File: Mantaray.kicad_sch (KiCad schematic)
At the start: 0 parts

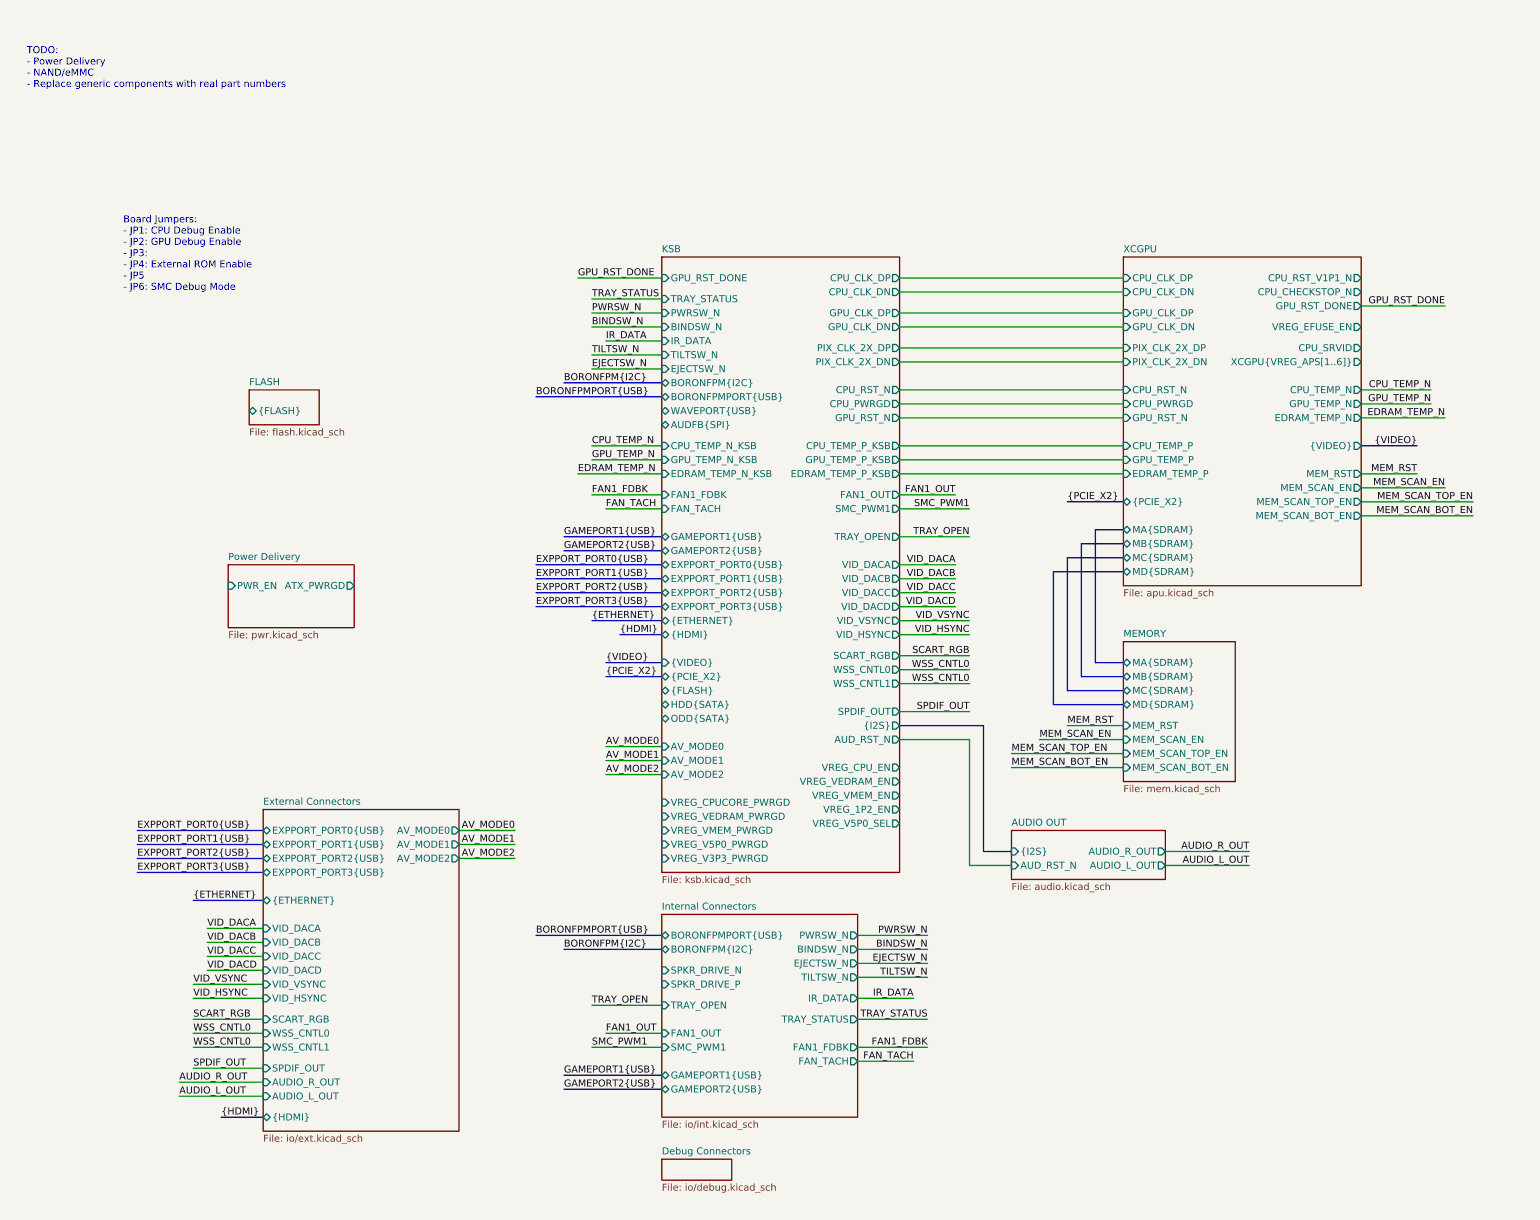
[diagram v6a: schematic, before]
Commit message: Nand Flash, Sata Connectors and removing (hopefully) unnecessary things
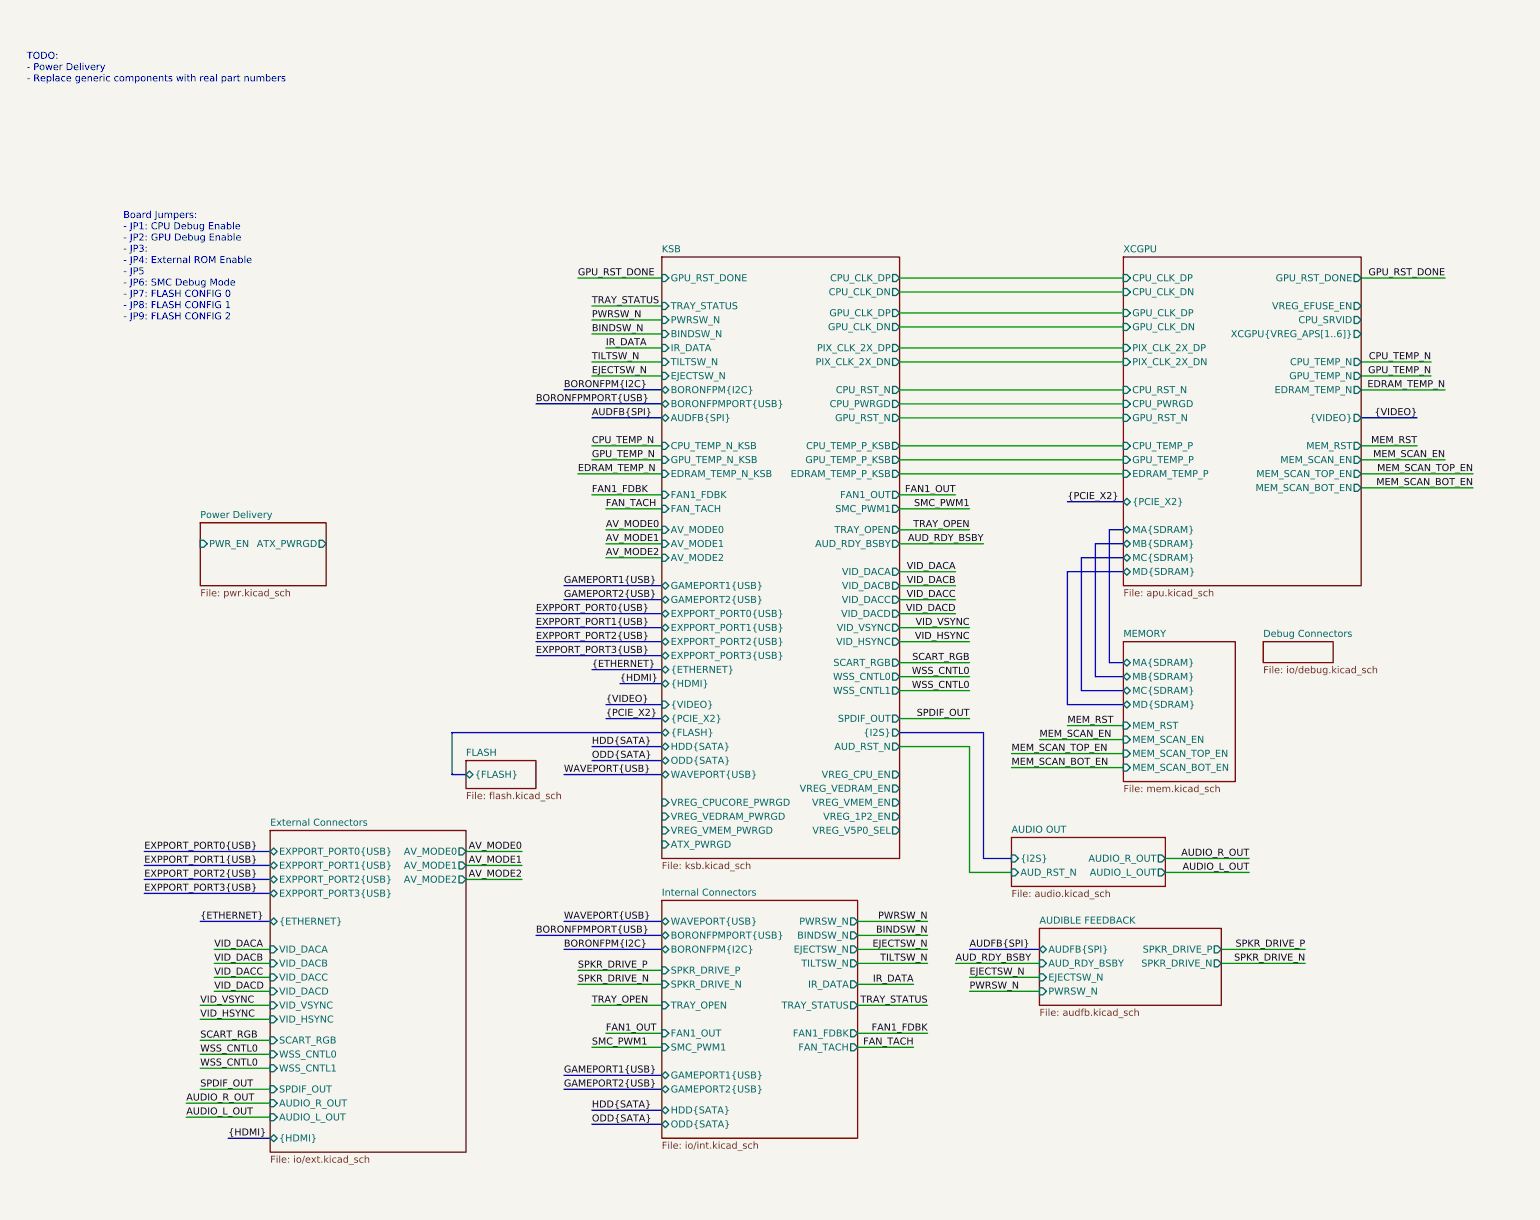
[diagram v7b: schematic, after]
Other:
- added sheet AUDIBLE FEEDBACK (audfb.kicad_sch)
- sheet Internal Connectors ports: added HDD{SATA}, ODD{SATA}, WAVEPORT{USB}; removed none
- sheet KSB ports: added ATX_PWRGD, AUD_RDY_BSBY; removed VREG_V3P3_PWRGD, VREG_V5P0_PWRGD
- sheet XCGPU ports: added none; removed CPU_CHECKSTOP_N, CPU_RST_V1P1_N
- note added: "Board Jumpers: - JP1: CPU Debug Enable - JP2: GPU Debug Enable - JP3: - JP4: External ROM Enable - JP5 - JP6: SMC Debug Mode - JP7: FLASH CONFIG 0 - JP8: FLASH CONFIG 1 - JP9: FLASH CONFIG 2"
- note added: "TODO: - Power Delivery - Replace generic components with real part numbers"
- note removed: "Board Jumpers: - JP1: CPU Debug Enable - JP2: GPU Debug Enable - JP3: - JP4: External ROM Enable - JP5 - JP6: SMC Debug Mode"
- note removed: "TODO: - Power Delivery - NAND/eMMC - Replace generic components with real part numbers"

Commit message: Multipurpose and standby power rails, Reannotated schematic
Added V_1P2, V_1P8, V_5P0DUAL, V_EFUSE, V_GPUPCIE, V_3P3STBY and V_1P2STBY
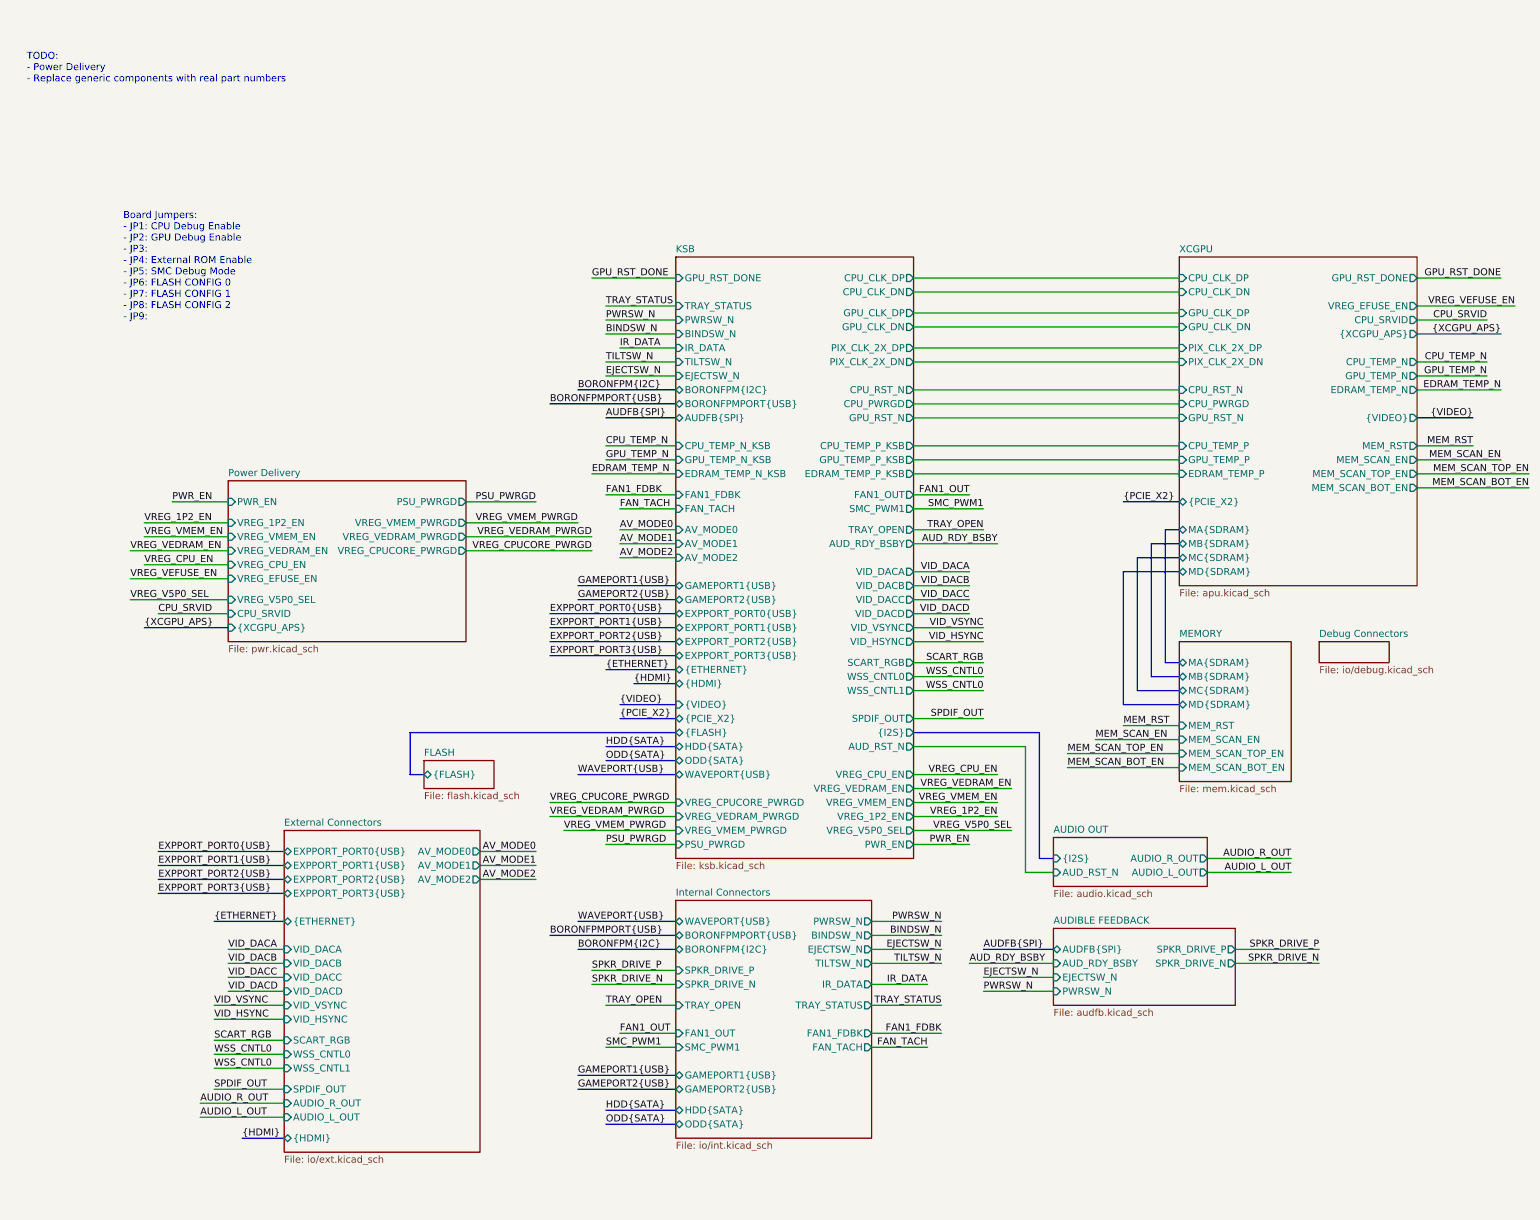
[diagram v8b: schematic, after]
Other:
- sheet KSB ports: added PSU_PWRGD, PWR_EN; removed ATX_PWRGD
- sheet Power Delivery ports: added CPU_SRVID, PSU_PWRGD, VREG_1P2_EN, VREG_CPUCORE_PWRGD, VREG_CPU_EN, VREG_EFUSE_EN, VREG_V5P0_SEL, VREG_VEDRAM_EN, VREG_VEDRAM_PWRGD, VREG_VMEM_EN, VREG_VMEM_PWRGD, {XCGPU_APS}; removed ATX_PWRGD
- sheet XCGPU ports: added {XCGPU_APS}; removed XCGPU{VREG_APS[1..6]}
- note added: "Board Jumpers: - JP1: CPU Debug Enable - JP2: GPU Debug Enable - JP3: - JP4: External ROM Enable - JP5: SMC Debug Mode - JP6: FLASH CONFIG 0 - JP7: FLASH CONFIG 1 - JP8: FLASH CONFIG 2 - JP9:"
- note removed: "Board Jumpers: - JP1: CPU Debug Enable - JP2: GPU Debug Enable - JP3: - JP4: External ROM Enable - JP5 - JP6: SMC Debug Mode - JP7: FLASH CONFIG 0 - JP8: FLASH CONFIG 1 - JP9: FLASH CONFIG 2"
